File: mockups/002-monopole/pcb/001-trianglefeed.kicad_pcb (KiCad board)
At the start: 2 copper layers, 55 x 120 mm, 10 parts, among them P1 SMA, P2 SMA

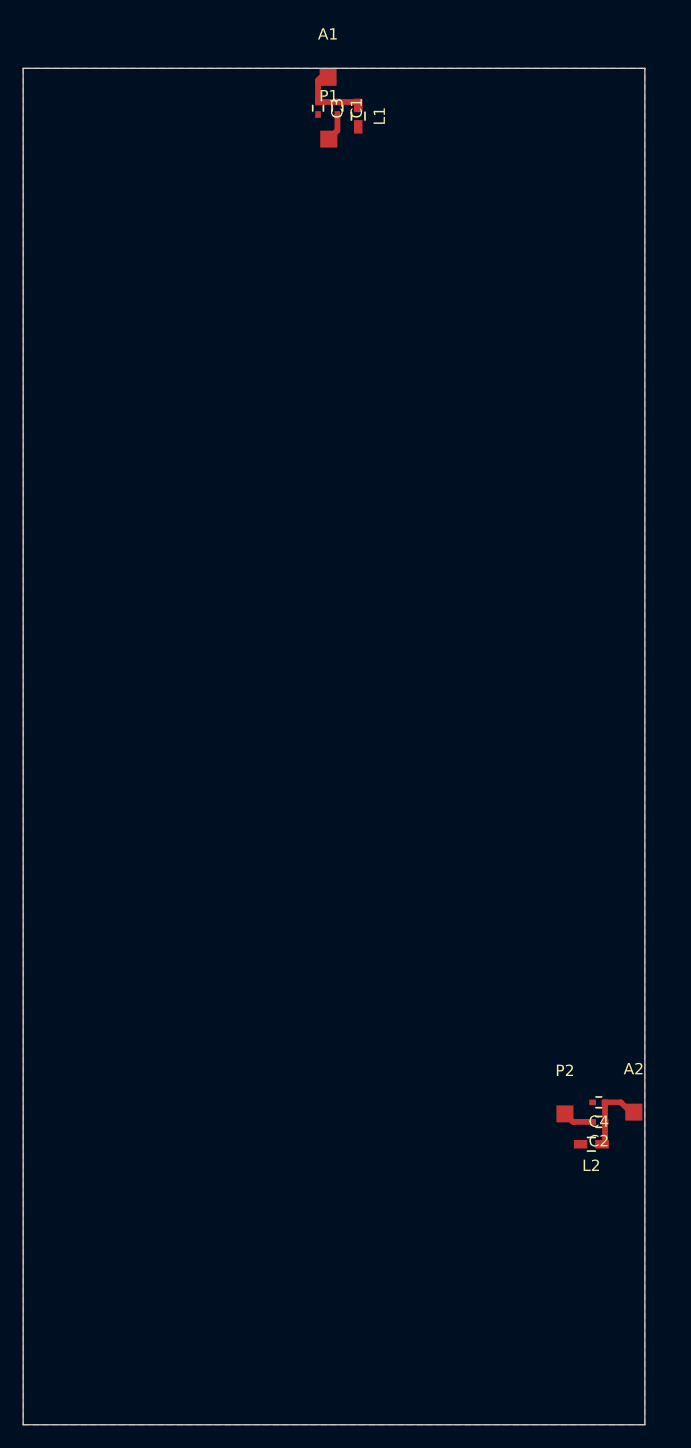
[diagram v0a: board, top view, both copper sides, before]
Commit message: 
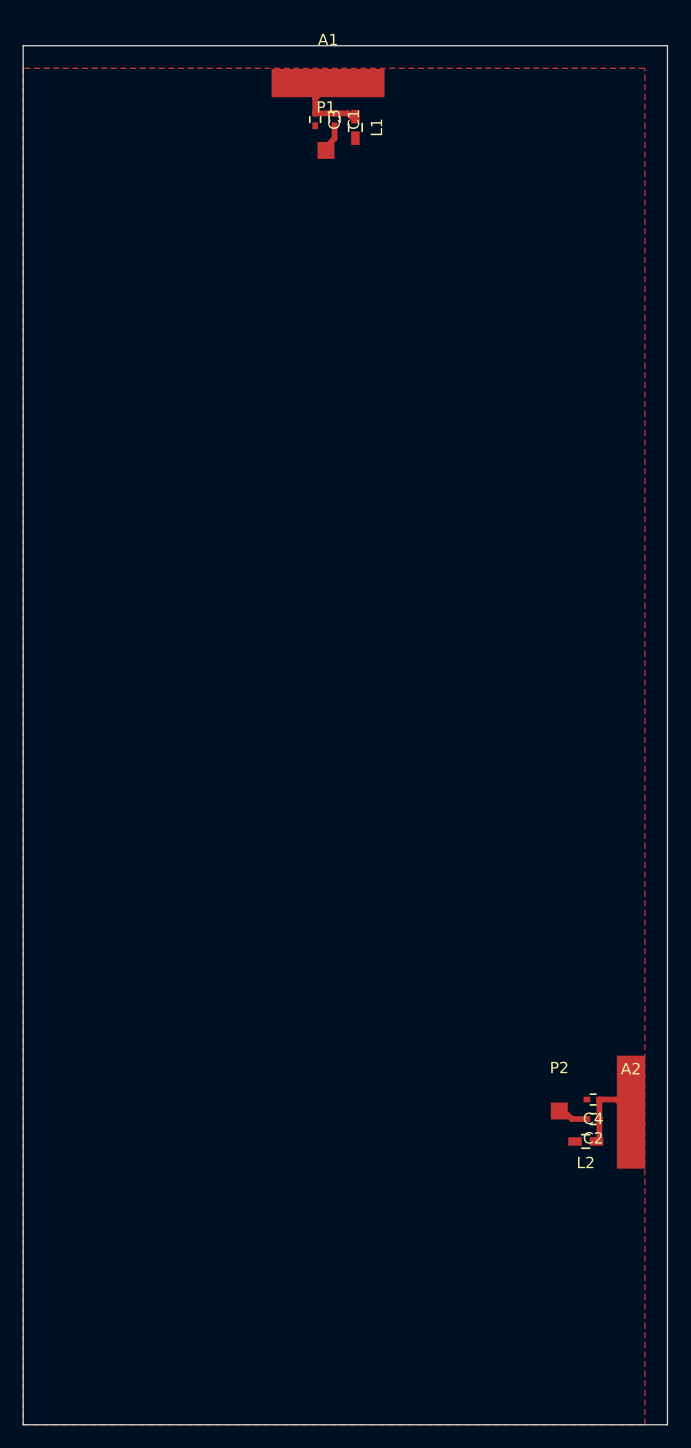
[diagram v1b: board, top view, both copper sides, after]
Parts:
- moved C1 1.03 mm to (54.6, 54.5)
- moved C3 1.03 mm to (52.8, 54.5)
- moved L1 1.03 mm to (56.4, 55.2)
- moved P1 1.03 mm to (53.8, 57.3)
- moved C2 0.56 mm to (77.4, 143.0)
- moved C4 0.56 mm to (77.4, 141.2)
- moved L2 0.56 mm to (76.8, 144.9)
- moved P2 0.56 mm to (74.4, 142.2)
- moved A1 0.50 mm to (54.0, 51.3)
- moved A2 0.25 mm to (80.8, 142.3)
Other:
- board size 55 x 120 mm -> 57 x 122 mm
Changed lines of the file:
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@@
     (links 11)
     (no_connects 0)
-    (area 26.899999 39.899999 176.920002 170.050001)
+    (area 26.949999 47.949999 84.050001 170.050001)
     (thickness 1.6)
     (drawings 25)
-    (tracks 17)
+    (tracks 19)
     (zones 0)
     (modules 10)
@@
     (38 B.Mask user)
     (39 F.Mask user)
-    (40 Dwgs.User user)
+    (40 Dwgs.User user hide)
     (41 Cmts.User user)
     (42 Eco1.User user)
@@
     (mod_text_size 1 1)
     (mod_text_width 0.15)
-    (pad_size 1.5 1.5)
-    (pad_drill 0.6)
+    (pad_size 2.5 10)
+    (pad_drill 0)
     (pad_to_mask_clearance 0)
     (aux_axis_origin 0 0)
-    (visible_elements FFFFFF5F)
+    (visible_elements 7FFFEFFF)
     (pcbplotparams
       (layerselection 0x00030_80000001)
@@
   )
   (module Measurement_Points:Measurement_Point_Square-SMD-Pad_Small (layer F.Cu)
-    (at 53.975 50.8)
+    (at 53.975 51.3)
     (descr "Mesurement Point, Square, SMD Pad,  1.5mm x 1.5mm,")
     (tags "Mesurement Point, Square, SMD Pad, 1.5mm x 1.5mm,")
@@
       (effects (font (size 1 1) (thickness 0.15)))
     )
-    (pad 1 smd rect (at 0 0) (size 1.50114 1.50114) (layers F.Cu F.Mask)
+    (pad 1 smd rect (at 0 0) (size 10 2.5) (layers F.Cu F.Mask)
       (net 1 /Ant1))
   )
   (module Measurement_Points:Measurement_Point_Square-SMD-Pad_Small (layer F.Cu)
-    (at 81.019762 142.345)
+    (at 80.769762 142.345)
     (descr "Mesurement Point, Square, SMD Pad,  1.5mm x 1.5mm,")
     (tags "Mesurement Point, Square, SMD Pad, 1.5mm x 1.5mm,")
@@
       (effects (font (size 1 1) (thickness 0.15)))
     )
-    (pad 1 smd rect (at 0 0) (size 1.50114 1.50114) (layers F.Cu F.Mask)
+    (pad 1 smd rect (at 0 0) (size 2.5 10) (layers F.Cu F.Mask)
       (net 2 /Ant2))
   )
   (module Capacitors_SMD:C_0402 (layer F.Cu)
-    (at 54.8005 53.5305 270)
+    (at 54.5505 54.5305 270)
     (descr "Capacitor SMD 0402, reflow soldering, AVX (see smccp.pdf)")
     (tags "capacitor 0402")
@@
   )
   (module Capacitors_SMD:C_0402 (layer F.Cu)
-    (at 77.9272 143.2052 180)
+    (at 77.4272 142.9552 180)
     (descr "Capacitor SMD 0402, reflow soldering, AVX (see smccp.pdf)")
     (tags "capacitor 0402")
@@
   )
   (module Capacitors_SMD:C_0402 (layer F.Cu)
-    (at 53.086 53.5305 270)
+    (at 52.836 54.5305 270)
     (descr "Capacitor SMD 0402, reflow soldering, AVX (see smccp.pdf)")
     (tags "capacitor 0402")
@@
   )
   (module Capacitors_SMD:C_0402 (layer F.Cu)
-    (at 77.9272 141.478 180)
+    (at 77.4272 141.228 180)
     (descr "Capacitor SMD 0402, reflow soldering, AVX (see smccp.pdf)")
     (tags "capacitor 0402")
@@
   )
   (module Capacitors_SMD:C_0603_HandSoldering (layer F.Cu)
-    (at 56.642 54.229 270)
+    (at 56.392 55.229 270)
     (descr "Capacitor SMD 0603, hand soldering")
     (tags "capacitor 0603")
@@
   )
   (module Capacitors_SMD:C_0603_HandSoldering (layer F.Cu)
-    (at 77.2668 145.1864 180)
+    (at 76.7668 144.9364 180)
     (descr "Capacitor SMD 0603, hand soldering")
     (tags "capacitor 0603")
@@
   )
   (module Measurement_Points:Measurement_Point_Square-SMD-Pad_Small (layer F.Cu)
-    (at 54.0385 56.261)
+    (at 53.7885 57.261)
     (descr "Mesurement Point, Square, SMD Pad,  1.5mm x 1.5mm,")
     (tags "Mesurement Point, Square, SMD Pad, 1.5mm x 1.5mm,")
@@
   )
   (module Measurement_Points:Measurement_Point_Square-SMD-Pad_Small (layer F.Cu)
-    (at 74.93 142.494)
+    (at 74.43 142.244)
     (descr "Mesurement Point, Square, SMD Pad,  1.5mm x 1.5mm,")
     (tags "Mesurement Point, Square, SMD Pad, 1.5mm x 1.5mm,")
@@
       (net 4 "Net-(C2-Pad2)"))
   )
+  (gr_line (start 84 170) (end 84 48) (angle 90) (layer Edge.Cuts) (width 0.1))
   (gr_line (start 84 115.5) (end 84 141.5) (angle 90) (layer Dwgs.User) (width 0.2))
   (gr_line (start 89 115.5) (end 84 115.5) (angle 90) (layer Dwgs.User) (width 0.2))
@@
   (gr_line (start 27 40) (end 53.5 40) (angle 90) (layer Dwgs.User) (width 0.2))
   (gr_line (start 27 48) (end 27 40) (angle 90) (layer Dwgs.User) (width 0.2))
-  (gr_line (start 27 50) (end 27 170) (angle 90) (layer Edge.Cuts) (width 0.1))
-  (gr_line (start 82 50) (end 27 50) (angle 90) (layer Edge.Cuts) (width 0.1))
-  (gr_line (start 82 170) (end 82 50) (angle 90) (layer Edge.Cuts) (width 0.1))
-  (gr_line (start 27 170) (end 82 170) (angle 90) (layer Edge.Cuts) (width 0.1))
-  (segment (start 54.8005 52.9805) (end 56.3435 52.9805) (width 0.508) (layer F.Cu) (net 1) (status C00000))
-  (segment (start 56.3435 52.9805) (end 56.642 53.279) (width 0.508) (layer F.Cu) (net 1) (status C00000))
-  (segment (start 53.086 52.9805) (end 54.8005 52.9805) (width 0.508) (layer F.Cu) (net 1) (status C00000))
-  (segment (start 53.975 50.8) (end 53.34 50.8) (width 0.508) (layer F.Cu) (net 1) (status C00000))
-  (segment (start 53.34 50.8) (end 53.086 51.054) (width 0.508) (layer F.Cu) (net 1) (status 400000))
-  (segment (start 53.086 51.054) (end 53.086 52.9805) (width 0.508) (layer F.Cu) (net 1) (status 800000))
-  (segment (start 78.4772 143.2052) (end 78.4772 141.478) (width 0.508) (layer F.Cu) (net 2))
-  (segment (start 78.2168 145.1864) (end 78.3336 145.1864) (width 0.508) (layer F.Cu) (net 2))
-  (segment (start 78.3336 145.1864) (end 78.4772 145.0428) (width 0.508) (layer F.Cu) (net 2))
-  (segment (start 78.4772 145.0428) (end 78.4772 143.2052) (width 0.508) (layer F.Cu) (net 2))
-  (segment (start 81.019762 142.345) (end 80.75 142.345) (width 0.508) (layer F.Cu) (net 2))
-  (segment (start 80.75 142.345) (end 79.883 141.478) (width 0.508) (layer F.Cu) (net 2))
-  (segment (start 79.883 141.478) (end 78.4772 141.478) (width 0.508) (layer F.Cu) (net 2))
-  (segment (start 54.8005 54.0805) (end 54.8005 55.499) (width 0.508) (layer F.Cu) (net 3) (status 400000))
-  (segment (start 54.8005 55.499) (end 54.0385 56.261) (width 0.508) (layer F.Cu) (net 3) (status 800000))
-  (segment (start 77.3772 143.2052) (end 75.6412 143.2052) (width 0.508) (layer F.Cu) (net 4))
-  (segment (start 75.6412 143.2052) (end 74.93 142.494) (width 0.508) (layer F.Cu) (net 4))
+  (gr_line (start 27 48) (end 27 170) (angle 90) (layer Edge.Cuts) (width 0.1))
+  (gr_line (start 84 48) (end 27 48) (angle 90) (layer Edge.Cuts) (width 0.1))
+  (gr_line (start 27 170) (end 84 170) (angle 90) (layer Edge.Cuts) (width 0.1))
+  (segment (start 56.392 54.279) (end 56.029 54.279) (width 0.508) (layer F.Cu) (net 1) (status C00000))
+  (segment (start 56.029 54.279) (end 55.7305 53.9805) (width 0.508) (layer F.Cu) (net 1) (status 400000))
+  (segment (start 55.7305 53.9805) (end 54.5505 53.9805) (width 0.508) (layer F.Cu) (net 1) (status 800000))
+  (segment (start 54.5505 53.9805) (end 52.836 53.9805) (width 0.508) (layer F.Cu) (net 1) (status C00000))
+  (segment (start 53.975 51.3) (end 53.975 51.525) (width 0.508) (layer F.Cu) (net 1) (status C00000))
+  (segment (start 53.975 51.525) (end 52.836 52.664) (width 0.508) (layer F.Cu) (net 1) (status 400000))
+  (segment (start 52.836 52.664) (end 52.836 53.9805) (width 0.508) (layer F.Cu) (net 1) (status 800000))
+  (segment (start 77.9772 144.676) (end 77.7168 144.9364) (width 0.508) (layer F.Cu) (net 2))
+  (segment (start 77.9772 142.9552) (end 77.9772 144.676) (width 0.508) (layer F.Cu) (net 2))
+  (segment (start 77.9772 142.9552) (end 77.9772 141.228) (width 0.508) (layer F.Cu) (net 2))
+  (segment (start 80.769762 142.345) (end 80.595 142.345) (width 0.508) (layer F.Cu) (net 2))
+  (segment (start 80.595 142.345) (end 79.478 141.228) (width 0.508) (layer F.Cu) (net 2))
+  (segment (start 79.478 141.228) (end 77.9772 141.228) (width 0.508) (layer F.Cu) (net 2))
+  (segment (start 54.5505 55.0805) (end 54.5505 56.1995) (width 0.508) (layer F.Cu) (net 3) (status 400000))
+  (segment (start 54.5505 56.1995) (end 53.7885 56.9615) (width 0.508) (layer F.Cu) (net 3) (status 800000))
+  (segment (start 53.7885 56.9615) (end 53.7885 57.261) (width 0.508) (layer F.Cu) (net 3) (status C00000))
+  (segment (start 76.8772 142.9552) (end 75.5448 142.9552) (width 0.508) (layer F.Cu) (net 4) (status 400000))
+  (segment (start 75.5448 142.9552) (end 74.8336 142.244) (width 0.508) (layer F.Cu) (net 4) (status 800000))
+  (segment (start 74.8336 142.244) (end 74.43 142.244) (width 0.508) (layer F.Cu) (net 4) (status C00000))
   (zone (net 5) (net_name /GND) (layer F.Cu) (hatch edge 0.508)
     (connect_pads (clearance 0))
